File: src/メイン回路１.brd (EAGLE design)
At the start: 8 parts

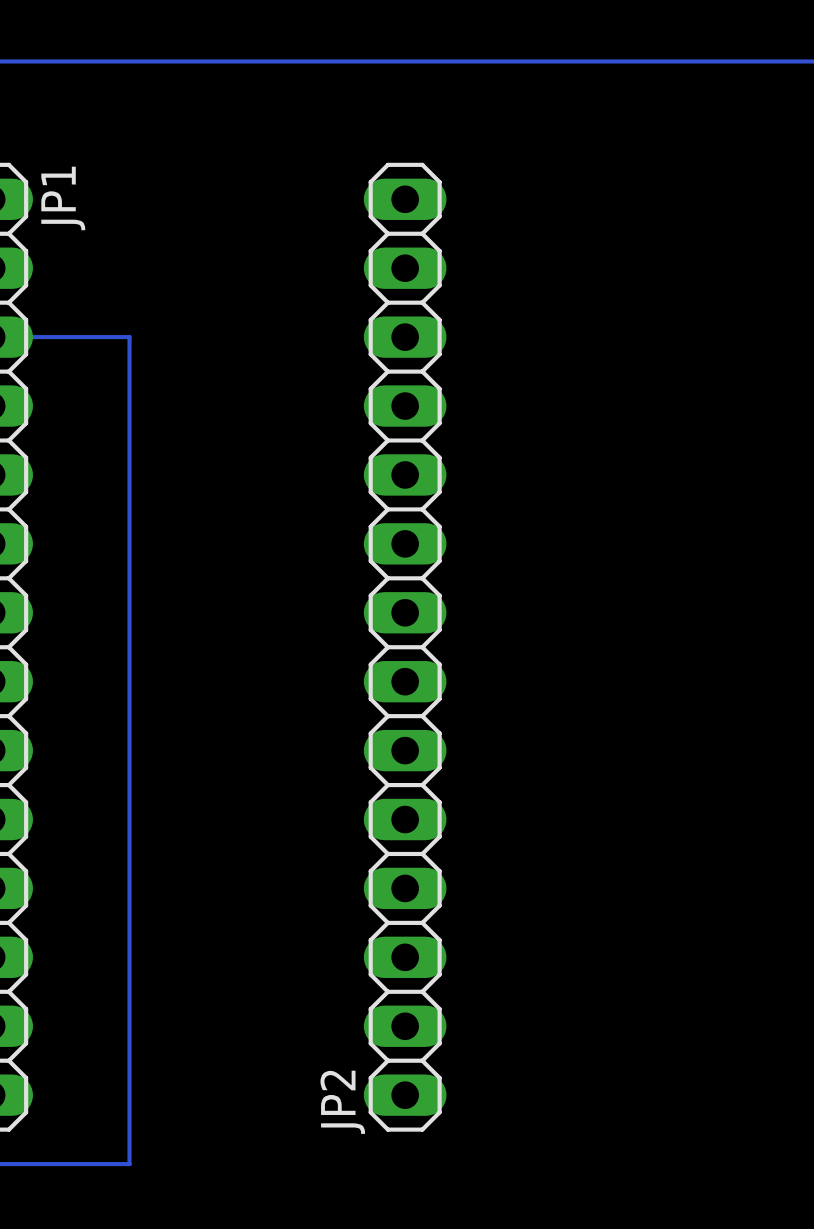
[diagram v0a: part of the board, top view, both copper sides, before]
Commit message: [move]ファイルの移動
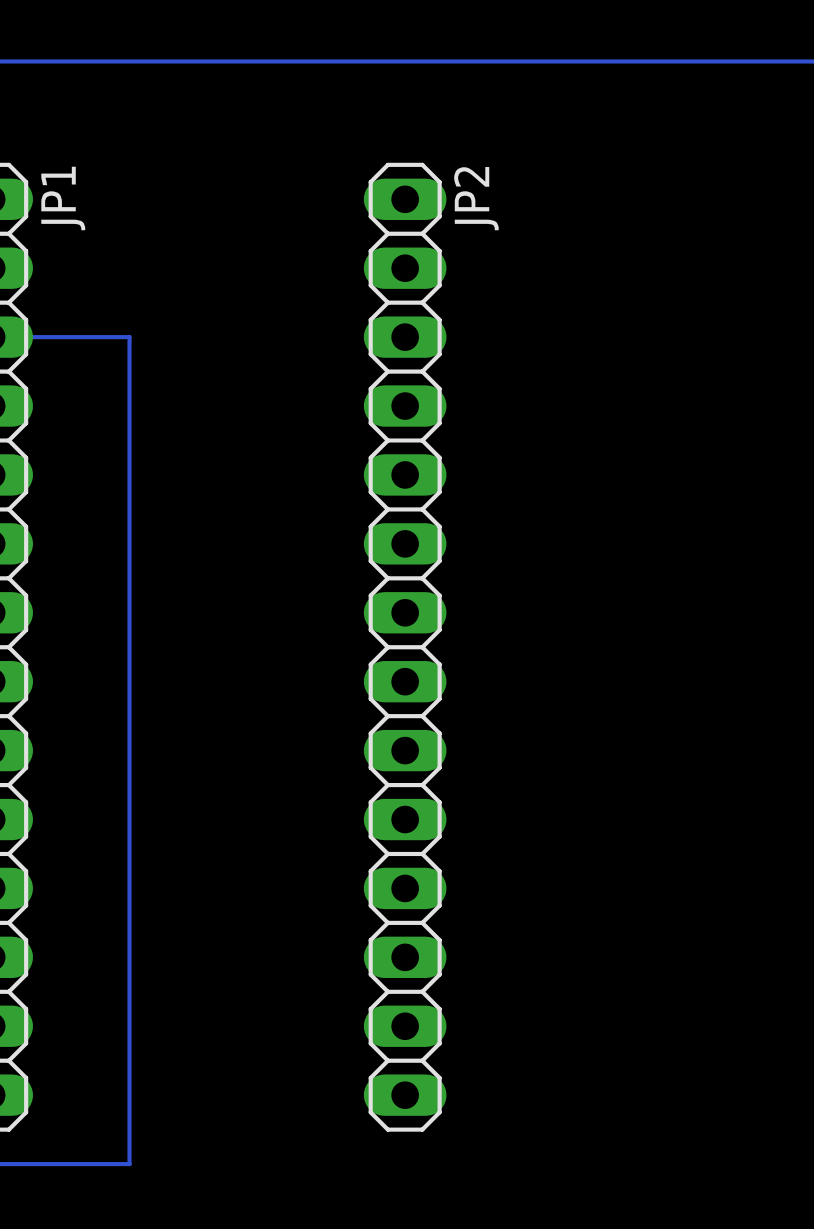
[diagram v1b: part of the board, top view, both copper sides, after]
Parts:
- turned JP2 to 270 degrees
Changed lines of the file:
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@@
 <attribute name="VALUE" x="-3.175" y="46.99" size="1.27" layer="27" rot="R270"/>
 </element>
-<element name="JP2" library="pinhead" library_urn="urn:adsk.eagle:library:325" package="1X14" package3d_urn="urn:adsk.eagle:package:22417/2" value="" x="15.24" y="29.21" smashed="yes" rot="R90">
-<attribute name="NAME" x="13.4112" y="11.3538" size="1.27" layer="25" ratio="10" rot="R90"/>
-<attribute name="POPULARITY" value="12" x="53.34" y="60.96" size="1.778" layer="27" rot="R90" display="off"/>
-<attribute name="VALUE" x="18.415" y="11.43" size="1.27" layer="27" rot="R90"/>
+<element name="JP2" library="pinhead" library_urn="urn:adsk.eagle:library:325" package="1X14" package3d_urn="urn:adsk.eagle:package:22417/2" value="" x="15.24" y="29.21" smashed="yes" rot="R270">
+<attribute name="NAME" x="17.0688" y="47.0662" size="1.27" layer="25" ratio="10" rot="R270"/>
+<attribute name="POPULARITY" value="12" x="-22.86" y="-2.54" size="1.778" layer="27" rot="R270" display="off"/>
+<attribute name="VALUE" x="12.065" y="46.99" size="1.27" layer="27" rot="R270"/>
 </element>
 <element name="JP3" library="pinhead" library_urn="urn:adsk.eagle:library:325" package="2X19" package3d_urn="urn:adsk.eagle:package:22500/2" value="" x="41.91" y="48.26" smashed="yes" rot="R270">

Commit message: メイン回路
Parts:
- removed JP1, JP2: (no value), pinhead:1X14
- removed SV1: (no value), con-ml:ML10
- removed U$1: 02-JST, con-jst-xh (1):B2B-XH
- added LED1: (no value), led:LED5MM
- added MCU_UART: 02-JST, con-jst-xh (1):B2B-XH
- added MDC: (no value), con-jst-xh:B4B-XH
- added PUB: (no value), con-ml:ML10
- added R1, R2, R3: 330, rcl:0204/7
- added R4, R5: 2.2k, rcl:0204/7
- added R6: 100, rcl:0204/7
- added TWE_L, TWE_R: (no value), pinhead:1X14
- moved U$2 12.5 mm to (-20.3, -8.89)
- moved U$3 11.4 mm to (128.3, -8.89)
- renumbered JP3 to F411RE_L, JP4 to F411RE_R
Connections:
- removed net N$1: F411RE_R.1, SV1.4
- removed net N$10: F411RE_R.10, SV1.1
- removed net N$11: F411RE_L.16, SV1.2
- removed net N$12: F411RE_L.2, U$1.2
- removed net N$13: F411RE_L.1, U$1.1
- removed net N$14: F411RE_L.15, JP1.3
- removed net N$15: F411RE_L.17, JP1.10
- removed net N$3: F411RE_R.5, SV1.8
- removed net N$4: F411RE_R.19, SV1.10
- removed net N$5: F411RE_R.37, SV1.3
- removed net N$6: F411RE_R.35, SV1.5
- removed net N$7: F411RE_R.33, SV1.7
- removed net N$8: F411RE_R.31, SV1.9
- new net 3V3: F411RE_L.16, PUB.2, TWE_R.1
- new net 5V: F411RE_L.18, MDC.1, R4.2, R5.2
- new net DIR1: F411RE_R.27, PUB.9
- new net DIR2: F411RE_R.25, PUB.7
- new net DIR3: F411RE_R.23, PUB.5
- new net GND: F411RE_L.20, F411RE_R.20, LED1.K, MDC.4, PUB.1, R1.1, R2.1, R3.1, TWE_L.1
- new net LED1: F411RE_R.11, R6.1
- new net PWM1: F411RE_R.29, PUB.10, R1.2
- new net PWM2: F411RE_R.31, PUB.8, R2.2
- new net PWM3: F411RE_R.33, PUB.6, R3.2
- new net RX: F411RE_L.17, TWE_L.3
- new net RX_MCU: F411RE_R.12, MCU_UART.2
- new net SCL: F411RE_R.3, MDC.3, R5.1
- new net SDA: F411RE_R.5, MDC.2, R4.1
- new net TX: F411RE_L.21, TWE_L.10
- new net TX_MCU: F411RE_R.14, MCU_UART.1
- net N$2: now also LED1.A, R6.2; no longer F411RE_R.3, SV1.6
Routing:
- net N$8: track 144.8 -> 0.00 mm
- net N$11: track 143.5 -> 0.00 mm, vias 2 -> 0
- net N$14: track 139.7 -> 0.00 mm
- net N$7: track 124.5 -> 0.00 mm
- net N$6: track 104.1 -> 0.00 mm
- net N$4: track 86.4 -> 0.00 mm
- net N$5: track 82.5 -> 0.00 mm
- net N$15: track 78.7 -> 0.00 mm
- net N$3: track 61.0 -> 0.00 mm
- net N$10: track 58.4 -> 0.00 mm
- net N$2: track 50.8 -> 0.00 mm
- net N$12: track 40.6 -> 0.00 mm
- net N$1: track 40.6 -> 0.00 mm
- net N$13: track 25.4 -> 0.00 mm

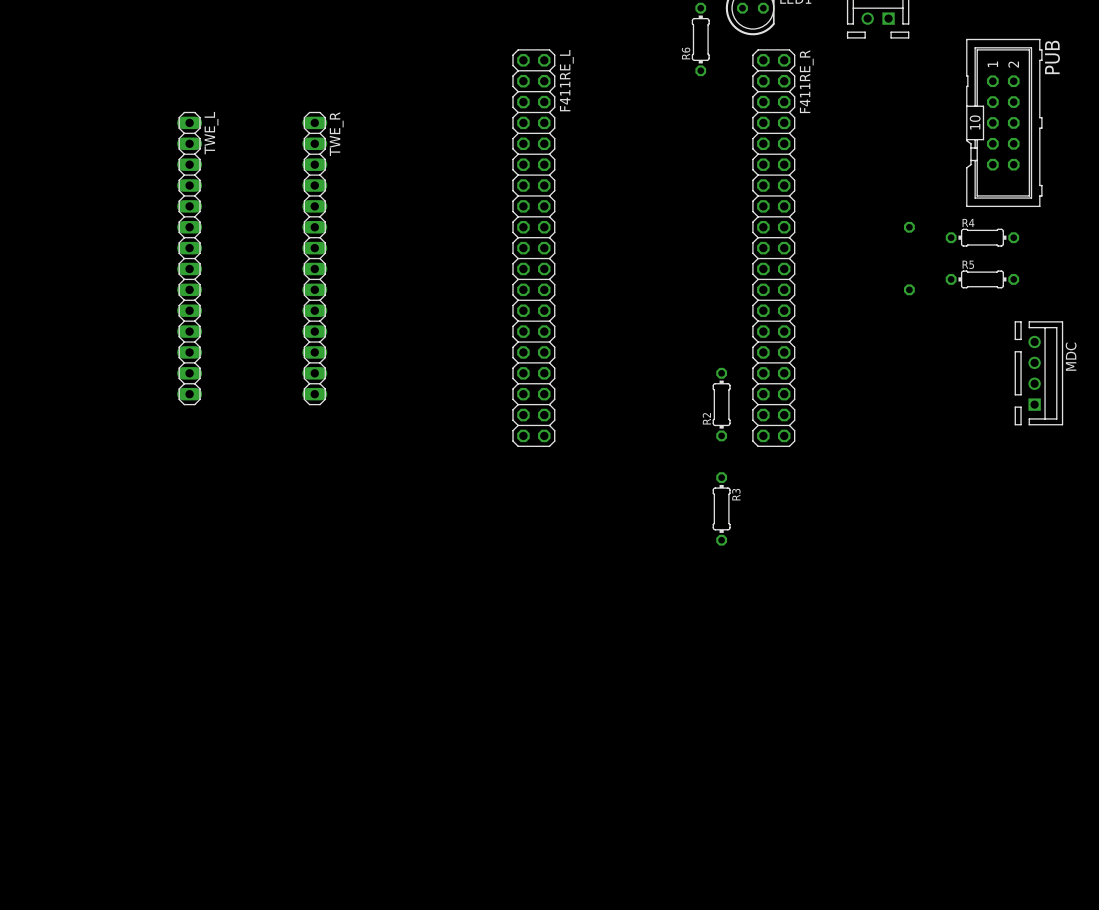
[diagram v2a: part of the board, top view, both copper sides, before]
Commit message: [fix]受信側の回路のsch修正全て
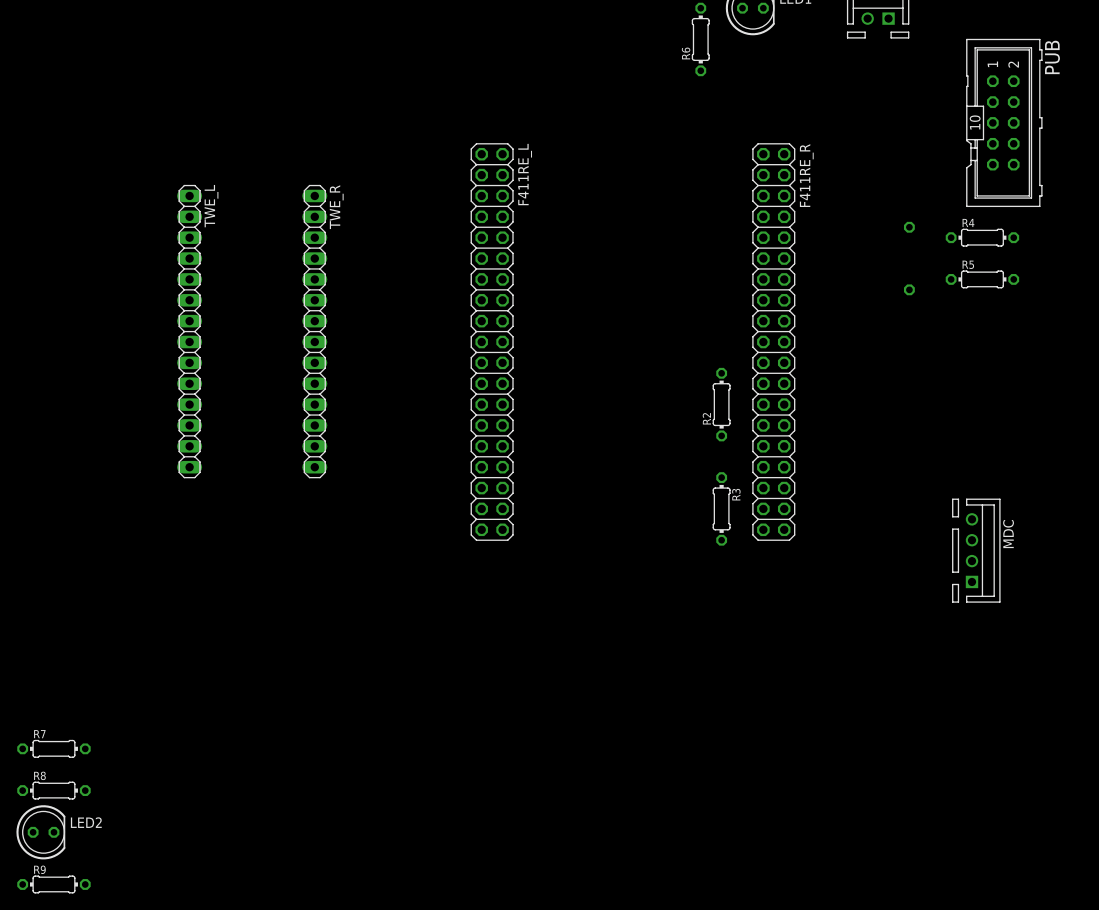
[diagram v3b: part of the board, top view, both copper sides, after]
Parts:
- added LED2: (no value), led:LED5MM
- added R7: 2.2k, rcl:0204/7
- added R8: 3.3k, rcl:0204/7
- added R9: 100, rcl:0204/7
- moved MDC 22.9 mm to (95.2, 11.4)
- moved F411RE_L 12.5 mm to (36.8, 36.8)
- moved F411RE_R 11.4 mm to (71.1, 36.8)
- moved TWE_L 8.89 mm to (0.00, 38.1)
- moved TWE_R 8.89 mm to (15.2, 38.1)
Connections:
- removed net 5V: F411RE_L.18, MDC.1, R4.2, R5.2
- new net 3V: PUB.2, R7.1, R8.2
- new net LED2: F411RE_R.21, R9.1
- new net N$1: LED2.A, R9.2
- new net U5V: F411RE_R.8, MDC.1, R4.2, R5.2, R7.2
- net 3V3: no longer PUB.2
- net GND: now also F411RE_L.22, LED2.K, R8.1

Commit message: [complete]メイン回路1の完成
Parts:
- removed U$3: (no value), prototyping-board (2):TYPE.B
- added LED3: (no value), led:LED5MM
- added R10: 100, rcl:0204/7
- added U$1: (no value), prototyping-board:TYPE.B
- U$2: device prototyping-board (2):TYPE.B -> prototyping-board:TYPE.B
- moved R8 154.7 mm to (118.1, 58.4)
- moved R7 152.8 mm to (121.9, 52.1), turned to 270 degrees
- moved U$2 152.5 mm to (132.1, -15.2), flipped to the top
- moved R9 97.6 mm to (14.0, 63.5), turned to 180 degrees
- moved LED2 86.4 mm to (11.4, 58.4)
- moved R3 63.8 mm to (119.4, 49.5)
- moved R2 55.0 mm to (116.8, 47.0), turned to 270 degrees
- moved LED1 50.7 mm to (21.6, 58.4), flipped to the bottom, turned to 180 degrees
- moved R4 46.4 mm to (104.1, 3.81), turned to 270 degrees
- moved R6 39.4 mm to (24.1, 63.5), turned to 180 degrees
- moved R5 31.4 mm to (104.1, 14.0), turned to 90 degrees
- moved R1 26.8 mm to (114.3, 44.5), flipped to the top
- moved PUB 19.9 mm to (108.0, 45.7)
- moved MCU_UART 19.1 mm to (95.2, 61.0)
- moved TWE_L 19.1 mm to (0.00, 19.1)
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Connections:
- new net LED3: F411RE_L.32, R10.1
- new net N$3: LED3.A, R10.2
- net DIR1: now also F411RE_R.29; no longer F411RE_R.27
- net DIR2: now also F411RE_R.31; no longer F411RE_R.25
- net DIR3: now also F411RE_R.33; no longer F411RE_R.23
- net GND: now also LED3.K, PUB.3, PUB.4
- net LED1: now also F411RE_L.28; no longer F411RE_R.11
- net LED2: now also F411RE_L.30; no longer F411RE_R.21
- net PWM1: now also F411RE_R.27; no longer F411RE_R.29
- net PWM2: now also F411RE_R.25; no longer F411RE_R.31
- net PWM3: now also F411RE_R.23; no longer F411RE_R.33
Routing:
- net GND: track 0.00 -> 266.3 mm
- net U5V: track 0.00 -> 170.2 mm, vias 0 -> 2
- net SDA: track 0.00 -> 167.6 mm
- net PWM3: track 0.00 -> 167.6 mm
- net SCL: track 0.00 -> 147.3 mm
- net PWM2: track 0.00 -> 147.3 mm
- net PWM1: track 0.00 -> 127.0 mm
- net LED3: track 0.00 -> 114.3 mm
- net DIR1: track 0.00 -> 101.6 mm
- net RX: track 0.00 -> 99.1 mm
- net DIR2: track 0.00 -> 91.4 mm
- net LED2: track 0.00 -> 91.4 mm
- net TX: track 0.00 -> 81.3 mm
- net DIR3: track 0.00 -> 81.3 mm
- net LED1: track 0.00 -> 68.6 mm
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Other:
- board text added: "MCU"
- board text added: "MDC"
- board text added: "TWE"
